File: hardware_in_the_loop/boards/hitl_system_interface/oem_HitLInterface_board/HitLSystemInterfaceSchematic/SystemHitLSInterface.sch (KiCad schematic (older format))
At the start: 50 parts, among them J1 CONN_02X03, J2 Conn_01x04_Female, J3 Conn_01x04_Female, J4 Barrel_Jack, J5 Conn_01x04_Female, U1 ATmega328P-AU, U2 TPS560430YF, U3 USB_MicroB, U4 FT232RL, U5 LM3480, U6 NanoFit_RA_TH_12, Y1 Crystal_SMD

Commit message: Updated Schematic with Changes From 2/9/21 DR
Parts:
- removed C13, C14: C_0.1uF, footprints:C_0805_OEM, symbol formula:C_0.1uF
- removed U5: LM3480, footprints:SOT-23-3_OEM, symbol formula:LM3480
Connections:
- net +3V3 is gone; now on net GND: J2.1 (Pin_1)
- net VCCUSB is gone; now on net VCC: C11.2, C12.2, D1.3 (K), U4.20 (VCC)
- net 12V: now also F2.1, J2.4 (Pin_4), J4.2
- net GND: now also D5.2 (A), J2.2 (Pin_2), J5.1 (Pin_1), J5.2 (Pin_2); no longer J2.4 (Pin_4)
- net VCC: no longer J2.2 (Pin_2), J4.2
- net SS_HitL: no longer names the net of U1.14 ((PCINT2/~SS~/OC1B)PB2)
- net SS_HitL: no longer J3.1 (Pin_1)
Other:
- note added: "Barrel jack should \nbe plugged into \n12 V power supply"
- note added: "MICROCONTROLLER"
- note added: "MISCELLANEOUS"
- note added: "Place Y1 near \npin 7 on Atmega"
- note added: "Place near \npin 4 on \nAtmega\n"
- note added: "Place near \npin 6 on \nAtmega"
- note added: "Place near pin \n20 on FTDI\n"
- note added: "Place near pin\n20 on FDTI"
- note removed: "5V IN"
- moved on the sheet: C10, C11, C12, C16, C2, C3, C4, C5, C6, C7, C8, C9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

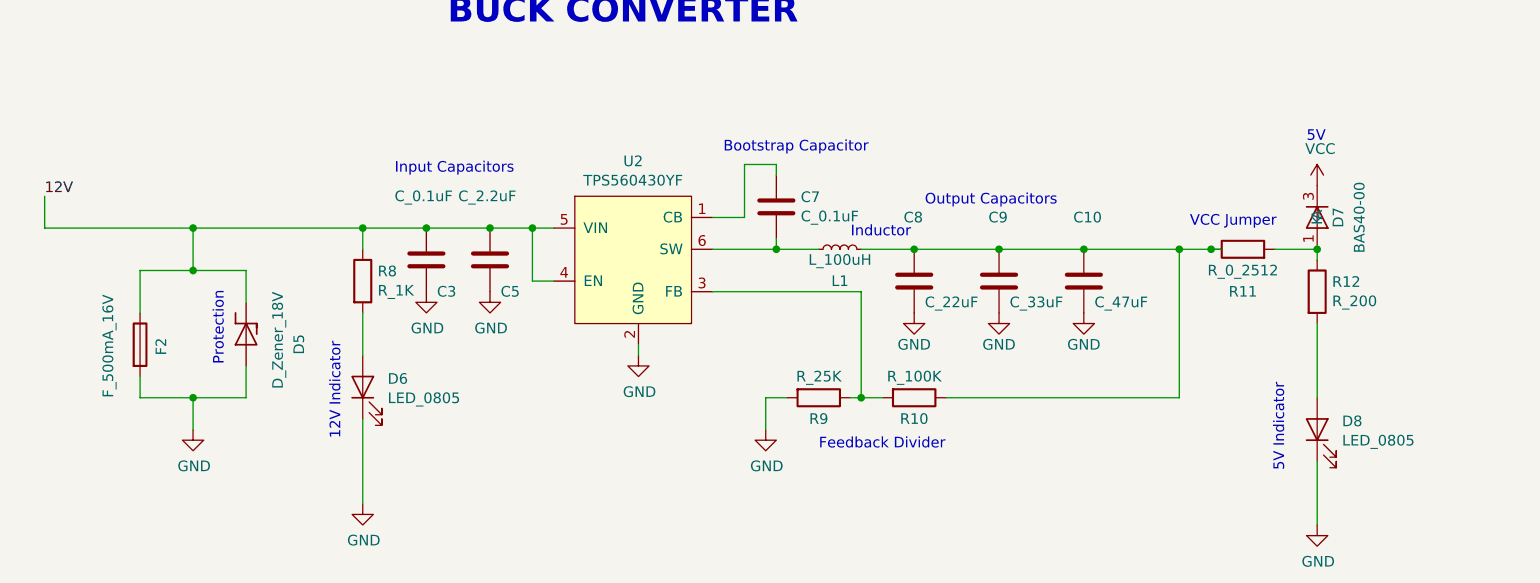
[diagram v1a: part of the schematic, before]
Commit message: Changed Buck Converter References
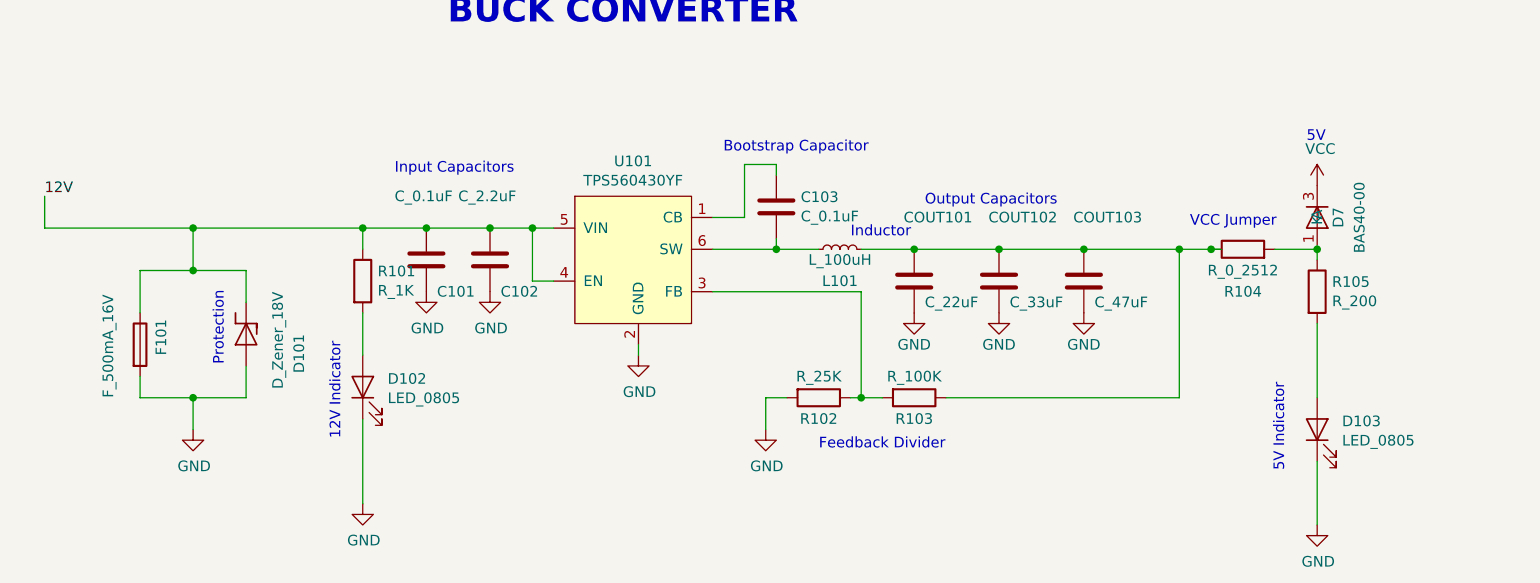
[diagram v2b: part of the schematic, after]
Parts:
- renumbered C3 to C101, C5 to C102, C7 to C103, C8 to COUT101, C9 to COUT102, C10 to COUT103, D5 to D101, D6 to D102, D8 to D103, F2 to F101, L1 to L101, R8 to R101, R9 to R102, R10 to R103, R11 to R104, R12 to R105, U2 to U101
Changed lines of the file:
@@
 $EndComp
 $Comp
-L formula:R_200 R12
+L formula:R_200 R105
 U 1 1 5FC841B9
 P 12750 6850
-F 0 "R12" H 12820 6896 50  0000 L CNN
+F 0 "R105" H 12820 6896 50  0000 L CNN
 F 1 "R_200" H 12820 6805 50  0000 L CNN
 F 2 "footprints:R_0805_OEM" H 12680 6850 50  0001 C CNN
@@
 Wire Wire Line
 	12750 7000 12750 7350
-$Comp
-L formula:LED_0805 D8
-U 1 1 5FC89372
-P 12750 7500
-F 0 "D8" V 12789 7383 50  0000 R CNN
-F 1 "LED_0805" V 12698 7383 50  0000 R CNN
-F 2 "footprints:LED_0805_OEM" H 12650 7500 50  0001 C CNN
-F 3 "http://www.osram-os.com/Graphics/XPic9/00078860_0.pdf" H 12750 7600 50  0001 C CNN
-F 4 "DK" H 12750 7500 60  0001 C CNN "MFN"
-F 5 "475-1410-1-ND" H 12750 7500 60  0001 C CNN "MPN"
-F 6 "https://www.digikey.com/products/en?keywords=475-1410-1-ND" H 13150 8000 60  0001 C CNN "PurchasingLink"
-	1    12750 7500
-	0    -1   -1   0
-$EndComp
 Wire Wire Line
 	12750 7650 12750 7950
@@
 $EndComp
 $Comp
-L formula:F_500mA_16V F2
+L formula:F_500mA_16V F101
 U 1 1 5FCD25BC
 P 7200 7100
-F 0 "F2" V 7300 7050 50  0000 L CNN
+F 0 "F101" V 7300 7050 50  0000 L CNN
 F 1 "F_500mA_16V" V 7050 6850 50  0000 L CNN
 F 2 "footprints:Fuse_1210" V 7130 7100 50  0001 C CNN
@@
 	7450 7350 7450 7500
 $Comp
-L formula:D_Zener_18V D5
+L formula:D_Zener_18V D101
 U 1 1 5FCCB5C8
 P 7700 7050
-F 0 "D5" H 7700 7300 50  0000 L CNN
+F 0 "D101" H 7700 7300 50  0000 L CNN
 F 1 "D_Zener_18V" H 7500 7200 50  0000 L CNN
 F 2 "footprints:DO-214AA" H 7600 7050 50  0001 C CNN
@@
 	8250 7450 8250 7850
 $Comp
-L formula:LED_0805 D6
+L formula:LED_0805 D102
 U 1 1 5FCBEC4A
 P 8250 7300
-F 0 "D6" V 8289 7183 50  0000 R CNN
+F 0 "D102" V 8289 7183 50  0000 R CNN
 F 1 "LED_0805" V 8198 7183 50  0000 R CNN
 F 2 "footprints:LED_0805_OEM" H 8150 7300 50  0001 C CNN
@@
 	8250 6950 8250 7150
 $Comp
-L formula:R_1K R8
+L formula:R_1K R101
 U 1 1 5FCB9C68
 P 8250 6800
-F 0 "R8" H 8320 6846 50  0000 L CNN
+F 0 "R101" H 8320 6846 50  0000 L CNN
 F 1 "R_1K" H 8320 6755 50  0000 L CNN
 F 2 "footprints:R_0805_OEM" H 8180 6800 50  0001 C CNN
@@
 Connection ~ 8550 6550
 $Comp
-L formula:C_0.1uF C3
+L formula:C_0.1uF C101
 U 1 1 5FCAD196
 P 8550 6700
-F 0 "C3" H 8600 6550 50  0000 L CNN
+F 0 "C101" H 8600 6550 50  0000 L CNN
 F 1 "C_0.1uF" H 8400 7000 50  0000 L CNN
 F 2 "footprints:C_0805_OEM" H 8588 6550 50  0001 C CNN
@@
 Connection ~ 8850 6550
 $Comp
-L formula:C_2.2uF C5
+L formula:C_2.2uF C102
 U 1 1 5FCA8F86
 P 8850 6750
-F 0 "C5" H 8900 6650 50  0000 L CNN
+F 0 "C102" H 8900 6650 50  0000 L CNN
 F 1 "C_2.2uF" H 8700 7100 50  0000 L CNN
 F 2 "footprints:C_0805_OEM" H 8888 7350 50  0001 C CNN
@@
 	10250 7350 10150 7350
 $Comp
-L formula:R_25K R9
+L formula:R_25K R102
 U 1 1 5FC94DCF
 P 10400 7350
-F 0 "R9" V 10500 7350 50  0000 C CNN
+F 0 "R102" V 10500 7350 50  0000 C CNN
 F 1 "R_25K" V 10300 7350 50  0000 C CNN
 F 2 "footprints:R_0805_OEM" H 10450 6800 50  0001 C CNN
@@
 	10700 7350 10600 7350
 $Comp
-L formula:R_100K R10
+L formula:R_100K R103
 U 1 1 5FC8E606
 P 10850 7350
-F 0 "R10" V 10950 7350 50  0000 C CNN
+F 0 "R103" V 10950 7350 50  0000 C CNN
 F 1 "R_100K" V 10750 7350 50  0000 C CNN
 F 2 "footprints:R_0805_OEM" H 10780 7350 50  0001 C CNN
@@
 Connection ~ 12250 6650
 $Comp
-L formula:R_0_2512 R11
+L formula:R_0_2512 R104
 U 1 1 5FC7A3CD
 P 12400 6650
-F 0 "R11" V 12200 6650 50  0000 C CNN
+F 0 "R104" V 12200 6650 50  0000 C CNN
 F 1 "R_0_2512" V 12300 6650 50  0000 C CNN
 F 2 "footprints:R_2512_OEM" H 12330 6650 50  0001 C CNN
@@
 Connection ~ 11650 6650
 $Comp
-L formula:C_47uF C10
+L formula:C_47uF COUT103
 U 1 1 5FC6D205
 P 11650 6800
-F 0 "C10" H 11600 7100 50  0000 L CNN
+F 0 "COUT103" H 11600 7100 50  0000 L CNN
 F 1 "C_47uF" H 11700 6700 50  0000 L CNN
 F 2 "footprints:C_0805_OEM" H 11688 6650 50  0001 C CNN
@@
 Connection ~ 11250 6650
 $Comp
-L formula:C_33uF C9
+L formula:C_33uF COUT102
 U 1 1 5FC6C092
 P 11250 6800
-F 0 "C9" H 11200 7100 50  0000 L CNN
+F 0 "COUT102" H 11200 7100 50  0000 L CNN
 F 1 "C_33uF" H 11300 6700 50  0000 L CNN
 F 2 "footprints:Fuse_1812" H 11300 6400 50  0001 C CNN
@@
 Connection ~ 10850 6650
 $Comp
-L formula:C_22uF C8
+L formula:C_22uF COUT101
 U 1 1 5FC56FAB
 P 10850 6800
-F 0 "C8" H 10800 7100 50  0000 L CNN
+F 0 "COUT101" H 10800 7100 50  0000 L CNN
 F 1 "C_22uF" H 10900 6700 50  0000 L CNN
 F 2 "footprints:C_1206_OEM" H 10888 6650 50  0001 C CNN
@@
 	10600 6650 10850 6650
 $Comp
-L formula:L_100uH L1
+L formula:L_100uH L101
 U 1 1 5FC51FCD
 P 10500 6650
-F 0 "L1" H 10500 6500 50  0000 C CNN
+F 0 "L101" H 10500 6500 50  0000 C CNN
 F 1 "L_100uH" H 10500 6600 50  0000 C CNN
 F 2 "footprints:L_100uH_OEM" H 10400 6450 50  0001 C CNN
@@
 	10200 6600 10200 6650
 $Comp
-L formula:C_0.1uF C7
+L formula:C_0.1uF C103
 U 1 1 5FC4C080
 P 10200 6450
-F 0 "C7" H 10315 6496 50  0000 L CNN
+F 0 "C103" H 10315 6496 50  0000 L CNN
 F 1 "C_0.1uF" H 10315 6405 50  0000 L CNN
 F 2 "footprints:C_0805_OEM" H 10238 6300 50  0001 C CNN
@@
 	9900 6500 10050 6500
 $Comp
-L formula:TPS560430YF U2
+L formula:TPS560430YF U101
 U 1 1 5FC45CC5
 P 9500 6700
-F 0 "U2" H 9525 7165 50  0000 C CNN
+F 0 "U101" H 9525 7165 50  0000 C CNN
 F 1 "TPS560430YF" H 9525 7074 50  0000 C CNN
 F 2 "footprints:SOT-23-6_OEM" H 9450 7400 50  0001 C CNN
@@
 	4550 7400 4550 7550
 $Comp
-L power:GND #PWR?
+L power:GND #PWR0101
 U 1 1 6043F404
 P 4550 7550
-F 0 "#PWR?" H 4550 7300 50  0001 C CNN
+F 0 "#PWR0101" H 4550 7300 50  0001 C CNN
 F 1 "GND" H 4650 7450 50  0000 C CNN
 F 2 "" H 4550 7550 50  0001 C CNN
@@
 	4300 7400 4550 7400
 $Comp
-L power:GND #PWR?
+L power:GND #PWR0102
 U 1 1 60448B59
 P 4400 7550
-F 0 "#PWR?" H 4400 7300 50  0001 C CNN
+F 0 "#PWR0102" H 4400 7300 50  0001 C CNN
 F 1 "GND" H 4300 7450 50  0000 C CNN
 F 2 "" H 4400 7550 50  0001 C CNN
@@
 12V
 $Comp
-L power:GND #PWR?
+L power:GND #PWR0103
 U 1 1 6034A658
 P 3400 8650
-F 0 "#PWR?" H 3400 8400 50  0001 C CNN
+F 0 "#PWR0103" H 3400 8400 50  0001 C CNN
 F 1 "GND" H 3405 8477 50  0000 C CNN
 F 2 "" H 3400 8650 50  0001 C CNN
@@
 	3400 8500 3400 8600
 Connection ~ 3400 8600
+$Comp
+L formula:LED_0805 D103
+U 1 1 5FC89372
+P 12750 7500
+F 0 "D103" V 12789 7383 50  0000 R CNN
+F 1 "LED_0805" V 12698 7383 50  0000 R CNN
+F 2 "footprints:LED_0805_OEM" H 12650 7500 50  0001 C CNN
+F 3 "http://www.osram-os.com/Graphics/XPic9/00078860_0.pdf" H 12750 7600 50  0001 C CNN
+F 4 "DK" H 12750 7500 60  0001 C CNN "MFN"
+F 5 "475-1410-1-ND" H 12750 7500 60  0001 C CNN "MPN"
+F 6 "https://www.digikey.com/products/en?keywords=475-1410-1-ND" H 13150 8000 60  0001 C CNN "PurchasingLink"
+	1    12750 7500
+	0    -1   -1   0
+$EndComp
 $EndSCHEMATC
